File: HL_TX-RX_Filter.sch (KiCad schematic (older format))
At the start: 202 parts, among them J1 CNR1, J10 To Rx in, J11 CONN_01X03, J2 CNR3, J3 Antenna, J4 CNR2, J5 CNR4, J6 From Tx, J7 ICSP, J8 CONN_01X05, J9 SCL SDA, Q1 2N7002, Q2 2N7002, Q3 2N7002, Q4 2N7002, Q5 2N7002, Q6 2N7002, Q7 2N7002, Q8 2N7002, U1 ATMEGA328-AU, U10 PE4259, U11 PE4259, U12 PE4259, U2 PE4259, U3 PE4259, U4 PE4259, U5 PE4259, U6 PE4259, U7 PE4259, U8 PE4259, U9 PE4259

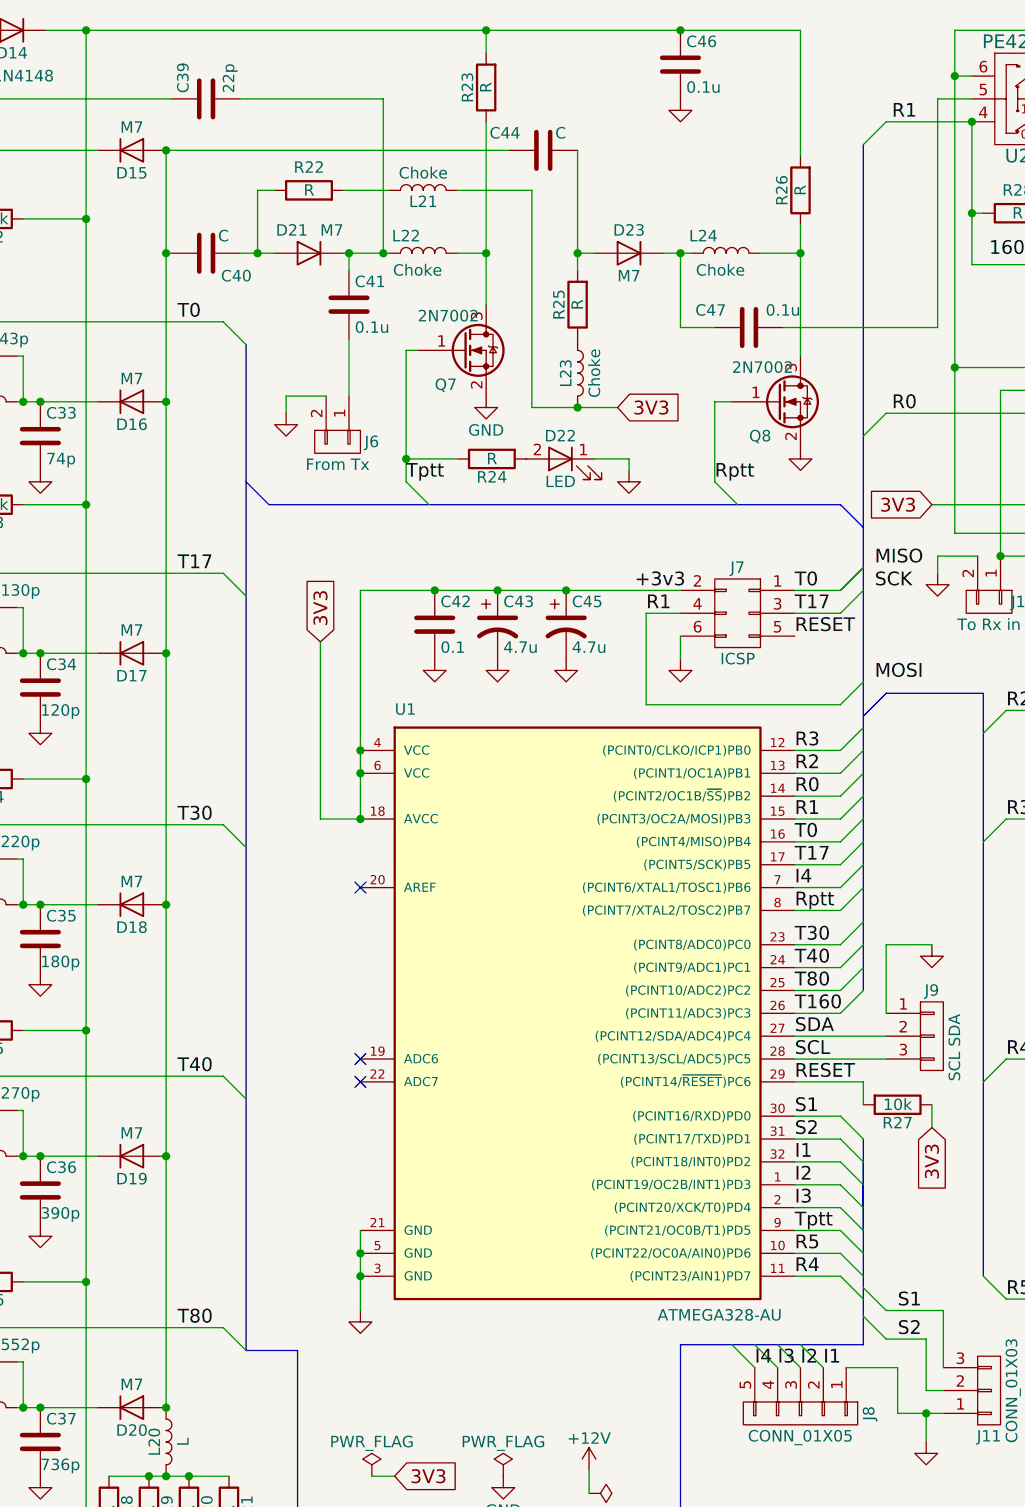
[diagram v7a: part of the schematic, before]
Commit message: Removed surplus choke etc from TX, RX switch
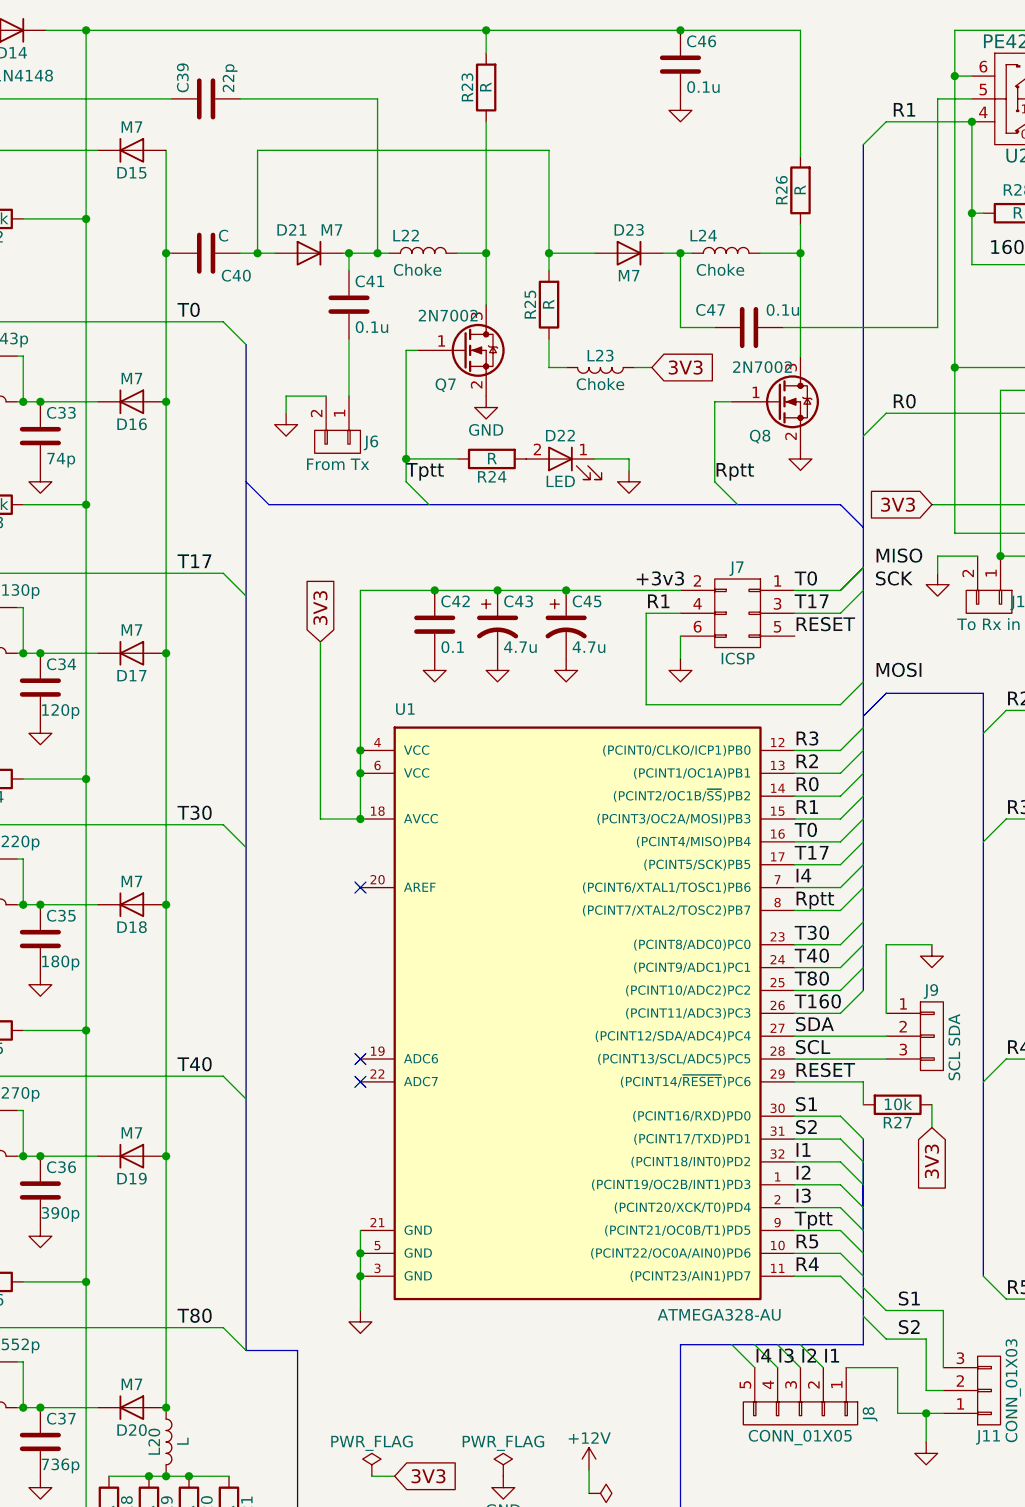
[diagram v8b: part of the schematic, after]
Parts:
- removed C44: C, Capacitors_SMD:C_1206_HandSoldering, symbol C
- removed L21: Choke, Inductors_G:BalunCoreChoke, symbol L
- removed R22: R, Resistors_SMD:R_1206_HandSoldering, symbol R
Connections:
- net 3V3: now also L23.1; no longer L23.2
- net at D23.2 (A), R25.2: now also C40.2, D21.2 (A)
- net at R25.1: now also L23.2; no longer L23.1
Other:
- moved on the sheet: L23, R25
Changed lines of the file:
@@
 L R R25
 U 1 1 591A7757
-P 6350 1800
-F 0 "R25" V 6430 1800 50  0000 C CNN
-F 1 "R" V 6350 1800 50  0000 C CNN
-F 2 "Resistors_SMD:R_1206_HandSoldering" V 6280 1800 50  0001 C CNN
-F 3 "" H 6350 1800 50  0001 C CNN
-	1    6350 1800
+P 6225 1800
+F 0 "R25" V 6305 1800 50  0000 C CNN
+F 1 "R" V 6225 1800 50  0000 C CNN
+F 2 "Resistors_SMD:R_1206_HandSoldering" V 6155 1800 50  0001 C CNN
+F 3 "" H 6225 1800 50  0001 C CNN
+	1    6225 1800
 	-1   0    0    1
 $EndComp
@@
 L L L23
 U 1 1 591A80A2
-P 6350 2100
-F 0 "L23" V 6300 2100 50  0000 C CNN
-F 1 "Choke" V 6425 2100 50  0000 C CNN
-F 2 "Inductors_G:BalunCoreChoke" H 6350 2100 50  0001 C CNN
-F 3 "" H 6350 2100 50  0001 C CNN
-	1    6350 2100
-	1    0    0    -1
-$EndComp
-$Comp
-L C C44
-U 1 1 591A91E5
-P 6200 1125
-F 0 "C44" V 6275 1225 50  0000 L CNN
-F 1 "C" V 6275 1025 50  0000 L CNN
-F 2 "Capacitors_SMD:C_1206_HandSoldering" H 6238 975 50  0001 C CNN
-F 3 "" H 6200 1125 50  0001 C CNN
-	1    6200 1125
-	0    -1   -1   0
+P 6450 2075
+F 0 "L23" V 6400 2075 50  0000 C CNN
+F 1 "Choke" V 6525 2075 50  0000 C CNN
+F 2 "Inductors_G:BalunCoreChoke" H 6450 2075 50  0001 C CNN
+F 3 "" H 6450 2075 50  0001 C CNN
+	1    6450 2075
+	0    1    1    0
 $EndComp
 $Comp
@@
 $EndComp
 $Comp
-L R R22
-U 1 1 591ABD0C
-P 5175 1300
-F 0 "R22" V 5275 1300 50  0000 C CNN
-F 1 "R" V 5175 1300 50  0000 C CNN
-F 2 "Resistors_SMD:R_1206_HandSoldering" V 5105 1300 50  0001 C CNN
-F 3 "" H 5175 1300 50  0001 C CNN
-	1    5175 1300
-	0    -1   -1   0
-$EndComp
-$Comp
-L L L21
-U 1 1 591ABD12
-P 5675 1300
-F 0 "L21" V 5625 1300 50  0000 C CNN
-F 1 "Choke" V 5750 1300 50  0000 C CNN
-F 2 "Inductors_G:BalunCoreChoke" H 5675 1300 50  0001 C CNN
-F 3 "" H 5675 1300 50  0001 C CNN
-	1    5675 1300
-	0    1    -1   0
-$EndComp
-$Comp
 L C C41
 U 1 1 591AE684
@@
 	1    0    0    -1
 $EndComp
-Text GLabel 6525 2250 2    60   Input ~ 0
+Text GLabel 6675 2075 2    60   Input ~ 0
 3V3
 Text GLabel 7900 2675 0    60   Input ~ 0
@@
 Connection ~ 1950 4950
 Wire Wire Line
-	4550 1125 6050 1125
+	4950 1125 6225 1125
 Connection ~ 4200 600
 Wire Wire Line
@@
 	6800 7650 6800 6350
 Wire Bus Line
-	6800 6350 7600 6350
+	7600 6350 6800 6350
 Wire Bus Line
-	7600 6350 7600 5450
+	7600 5450 7600 6350
 Wire Wire Line
 	4575 900  3725 900
@@
 	7300 6050 7500 6050
 Wire Wire Line
-	6350 1125 6350 1650
-Wire Wire Line
-	6425 1575 6350 1575
-Connection ~ 6350 1575
+	6225 1125 6225 1650
+Wire Wire Line
+	6425 1575 6225 1575
+Connection ~ 6225 1575
 Wire Wire Line
 	7325 600  7325 1150
@@
 	4875 1575 5025 1575
 Wire Wire Line
-	4875 900  5500 900
-Wire Wire Line
-	5500 900  5500 1575
-Connection ~ 5500 1575
+	4875 900  5475 900
+Wire Wire Line
+	5475 900  5475 1575
+Connection ~ 5475 1575
 Wire Wire Line
 	5350 1650 5350 1575
@@
 	5350 1950 5350 2200
 Wire Wire Line
-	5025 1300 4950 1300
-Wire Wire Line
-	4950 1300 4950 1575
+	4950 1125 4950 1575
 Connection ~ 4950 1575
-Wire Wire Line
-	5325 1300 5525 1300
-Wire Wire Line
-	5825 1300 6150 1300
-Wire Wire Line
-	6150 1300 6150 2250
-Wire Wire Line
-	6150 2250 6525 2250
 Wire Wire Line
 	7900 2675 8525 2675
@@
 Wire Wire Line
 	6800 3250 6800 3350
-Connection ~ 6350 2250
 Wire Wire Line
 	5400 5850 5400 6200
@@
 Wire Wire Line
 	4550 1125 4550 6625
-Connection ~ 4550 1125
 Wire Wire Line
 	7875 6650 7875 6775
@@
 	7500 5450 7600 5550
 Wire Bus Line
-	7600 5750 7600 5550
+	7600 5550 7600 5850
 Wire Bus Line
-	7600 5850 7600 5650
+	7600 5750 7600 5650
 $Comp
 L CONN_01X03 J9
@@
 Wire Wire Line
 	7700 4600 7900 4600
+Wire Wire Line
+	6225 1950 6225 2075
+Wire Wire Line
+	6225 2075 6300 2075
+Wire Wire Line
+	6600 2075 6675 2075
 $EndSCHEMATC
